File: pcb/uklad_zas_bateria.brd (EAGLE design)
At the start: 59.8 x 34 mm, 32 parts

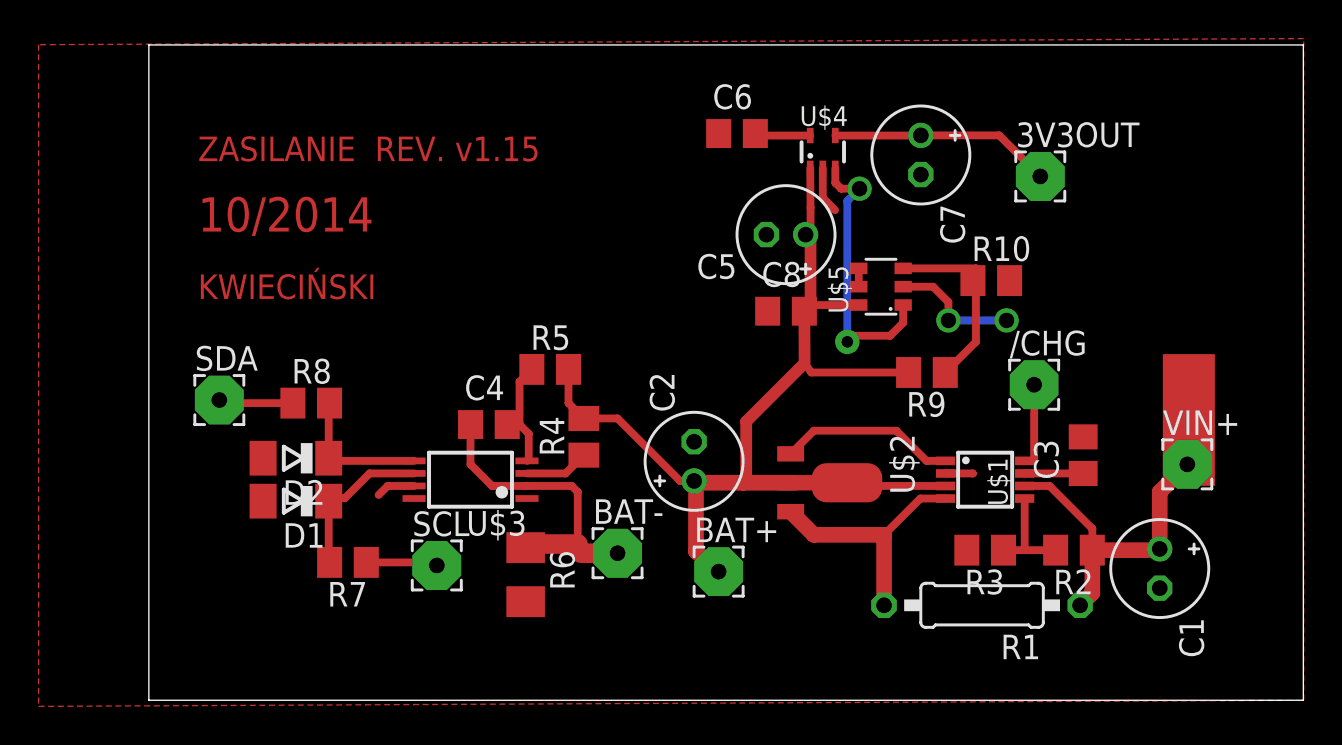
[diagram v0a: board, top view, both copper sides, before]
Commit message: dodanie worda z magisterką gdzie pisze na bierząco, update kosztorysu, nowe bordy
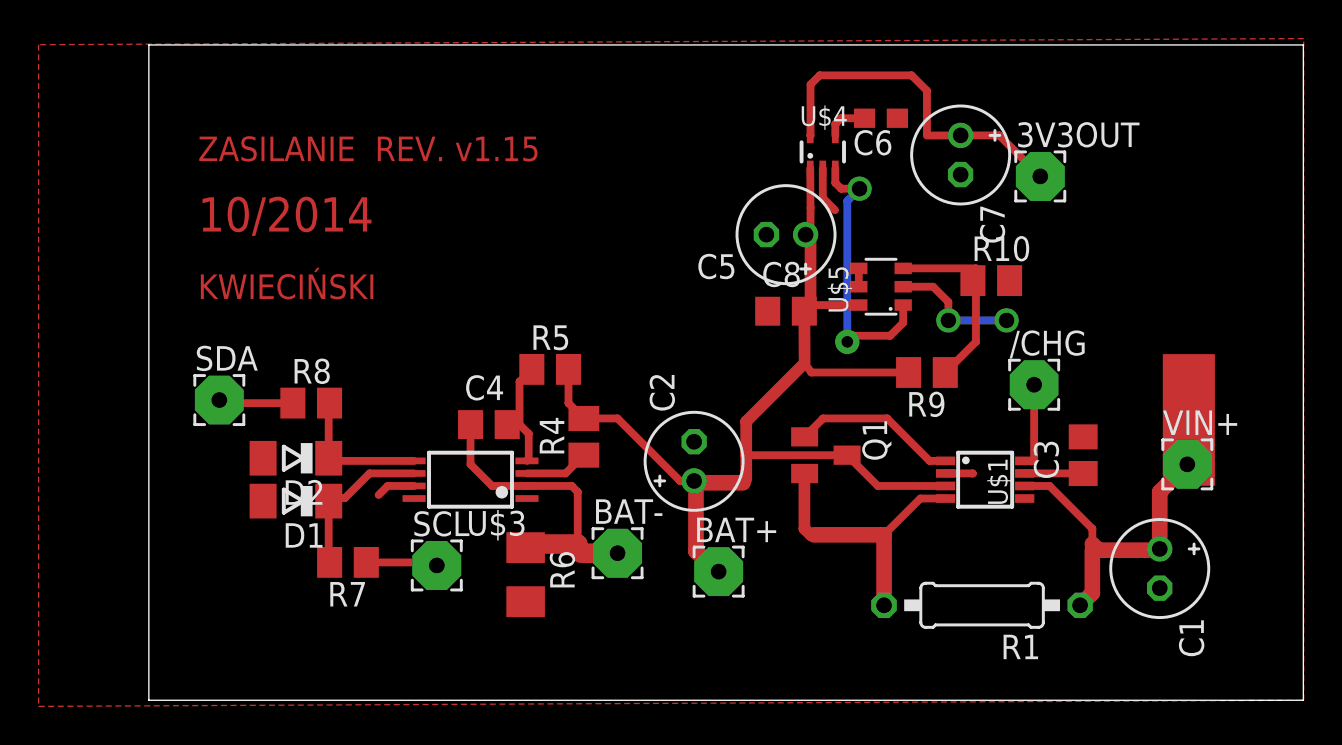
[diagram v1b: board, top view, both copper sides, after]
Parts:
- removed R2, R3: (no value), resistor:M0805
- removed U$2: BCX51, ref-packages:SOT89-BCE
- added Q1: AP2301, transistor-small-signal:SOT23
- C1: value (none) -> 10u
- C2: value (none) -> 33u
- C6: value 100n -> 10n; device rcl:C0805 -> rcl:C0603
- moved C6 7.50 mm to (23.8, 30.2), turned to 180 degrees
- moved C7 2.06 mm to (27.9, 28.3)
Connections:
- removed net N$7: R2.2, R3.1, U$1.5
- net GND: no longer R3.2
- net N$1: now also Q1.1; no longer U$2.B
- net N$19: now also Q1.3; no longer U$2.C
- net N$2: now also Q1.2; no longer U$2.E
- net N$3: no longer R2.1
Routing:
- net N$5: track 2.89 -> 11.4 mm
- net N$7: track 5.39 -> 0.00 mm
- net N$17: track 11.5 -> 8.89 mm
- net N$2: track 13.0 -> 14.7 mm
- net N$1: track 9.17 -> 8.61 mm
